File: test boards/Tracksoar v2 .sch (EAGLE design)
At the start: 47 parts, among them IC1 BME280, IC2 74AHC1G125DBV, Y1 16MHZ

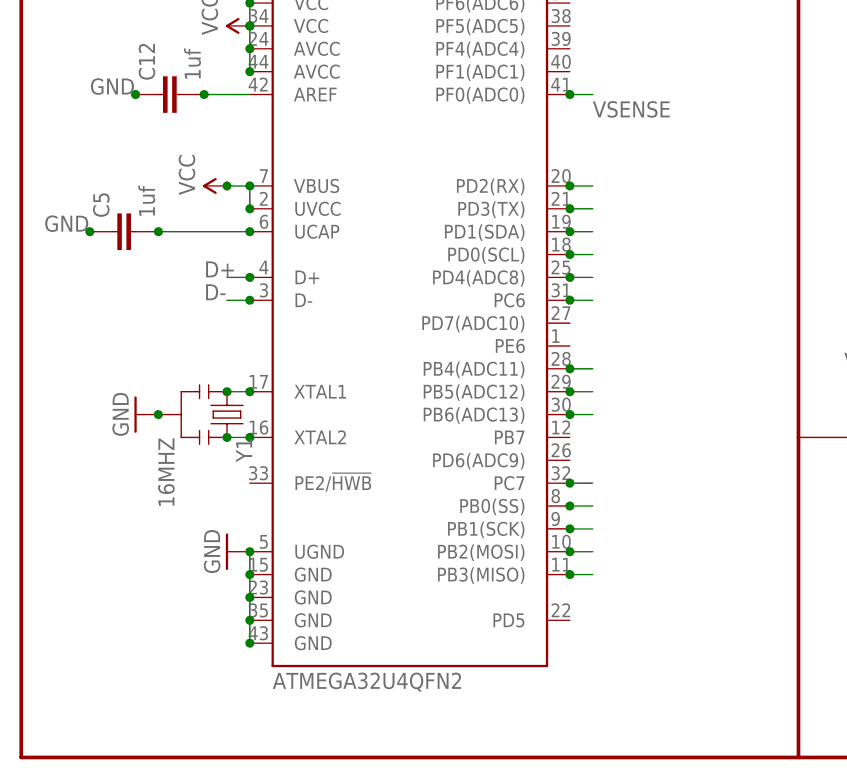
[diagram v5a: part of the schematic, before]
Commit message: Added Pull down to HWB pin
added a 10k pull down resistor to HWB to resolve issues flashing the
boot loader
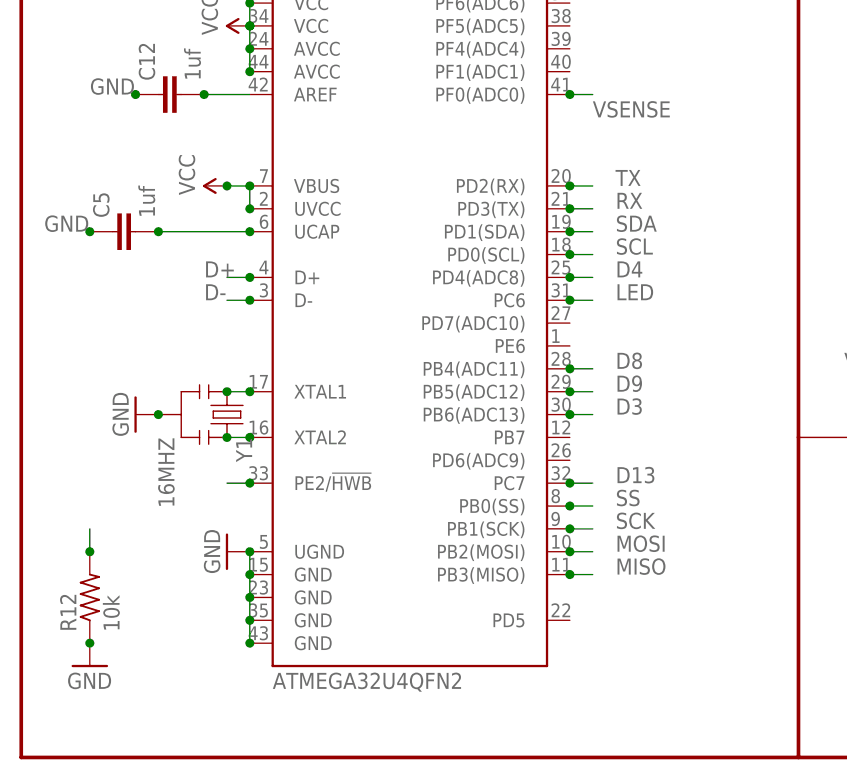
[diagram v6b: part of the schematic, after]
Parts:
- added R12: 10k, adafruit:R-US_R0402
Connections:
- new net HWB: R12.2, U$4.PE2/!HWB
- net GND: now also R12.1
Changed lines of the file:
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@@
 <part name="C14" library="SparkFun-Capacitors" deviceset="CAP" device="0402-CAP" value=".1uf"/>
 <part name="GND21" library="SparkFun-Aesthetics" deviceset="GND" device=""/>
+<part name="R12" library="adafruit" deviceset="R-US_" device="R0402" value="10k"/>
+<part name="GND23" library="SparkFun-Aesthetics" deviceset="GND" device=""/>
 </parts>
 <sheets>
@@
 <instance part="C14" gate="G$1" x="73.66" y="180.34" rot="R270"/>
 <instance part="GND21" gate="1" x="81.28" y="180.34" rot="R90"/>
+<instance part="R12" gate="G$1" x="7.62" y="17.78" rot="R90"/>
+<instance part="GND23" gate="1" x="7.62" y="10.16"/>
 </instances>
 <busses>
@@
 <junction x="78.74" y="180.34"/>
 </segment>
+<segment>
+<pinref part="R12" gate="G$1" pin="1"/>
+<pinref part="GND23" gate="1" pin="GND"/>
+<junction x="7.62" y="12.7"/>
+</segment>
 </net>
 <net name="D3" class="0">
@@
 <pinref part="U$4" gate="G$1" pin="PB6(ADC13)"/>
 <junction x="60.96" y="38.1"/>
+<label x="66.04" y="38.1" size="1.778" layer="95"/>
 </segment>
 </net>
@@
 <pinref part="U$4" gate="G$1" pin="PD4(ADC8)"/>
 <junction x="60.96" y="53.34"/>
+<label x="66.04" y="53.34" size="1.778" layer="95"/>
 </segment>
 </net>
@@
 <pinref part="U$4" gate="G$1" pin="PB3(MISO)"/>
 <junction x="60.96" y="20.32"/>
+<label x="66.04" y="20.32" size="1.778" layer="95"/>
 </segment>
 <segment>
@@
 <pinref part="U$4" gate="G$1" pin="PB2(MOSI)"/>
 <junction x="60.96" y="22.86"/>
+<label x="66.04" y="22.86" size="1.778" layer="95"/>
 </segment>
 <segment>
@@
 <pinref part="U$4" gate="G$1" pin="PB1(SCK)"/>
 <junction x="60.96" y="25.4"/>
+<label x="66.04" y="25.4" size="1.778" layer="95"/>
 </segment>
 <segment>
@@
 <pinref part="U$4" gate="G$1" pin="PB0(SS)"/>
 <junction x="60.96" y="27.94"/>
+<label x="66.04" y="27.94" size="1.778" layer="95"/>
 </segment>
 <segment>
@@
 <pinref part="U$4" gate="G$1" pin="PC6"/>
 <junction x="60.96" y="50.8"/>
+<label x="66.04" y="50.8" size="1.778" layer="95"/>
 </segment>
 </net>
@@
 <pinref part="U$4" gate="G$1" pin="PD1(SDA)"/>
 <junction x="60.96" y="58.42"/>
+<label x="66.04" y="58.42" size="1.778" layer="95"/>
 </segment>
 <segment>
@@
 <pinref part="U$4" gate="G$1" pin="PD0(SCL)"/>
 <junction x="60.96" y="55.88"/>
+<label x="66.04" y="55.88" size="1.778" layer="95"/>
 </segment>
 <segment>
@@
 <pinref part="U$4" gate="G$1" pin="PD2(RX)"/>
 <junction x="60.96" y="63.5"/>
+<label x="66.04" y="63.5" size="1.778" layer="95"/>
 </segment>
 <segment>
@@
 <pinref part="U$4" gate="G$1" pin="PD3(TX)"/>
 <junction x="60.96" y="60.96"/>
+<label x="66.04" y="60.96" size="1.778" layer="95"/>
 </segment>
 <segment>
@@
 <wire x1="60.96" y1="43.18" x2="63.5" y2="43.18" width="0.1524" layer="91"/>
 <junction x="60.96" y="43.18"/>
+<label x="66.04" y="43.18" size="1.778" layer="95"/>
 </segment>
 <segment>
@@
 <wire x1="60.96" y1="40.64" x2="63.5" y2="40.64" width="0.1524" layer="91"/>
 <junction x="60.96" y="40.64"/>
+<label x="66.04" y="40.64" size="1.778" layer="95"/>
 </segment>
 <segment>
@@
 <wire x1="60.96" y1="30.48" x2="63.5" y2="30.48" width="0.1524" layer="91"/>
 <junction x="60.96" y="30.48"/>
+<label x="66.04" y="30.48" size="1.778" layer="95"/>
 </segment>
 </net>
@@
 </segment>
 </net>
+<net name="HWB" class="0">
+<segment>
+<pinref part="U$4" gate="G$1" pin="PE2/!HWB"/>
+<wire x1="25.4" y1="30.48" x2="22.86" y2="30.48" width="0.1524" layer="91"/>
+<junction x="25.4" y="30.48"/>
+</segment>
+<segment>
+<pinref part="R12" gate="G$1" pin="2"/>
+<wire x1="7.62" y1="22.86" x2="7.62" y2="25.4" width="0.1524" layer="91"/>
+<junction x="7.62" y="22.86"/>
+</segment>
+</net>

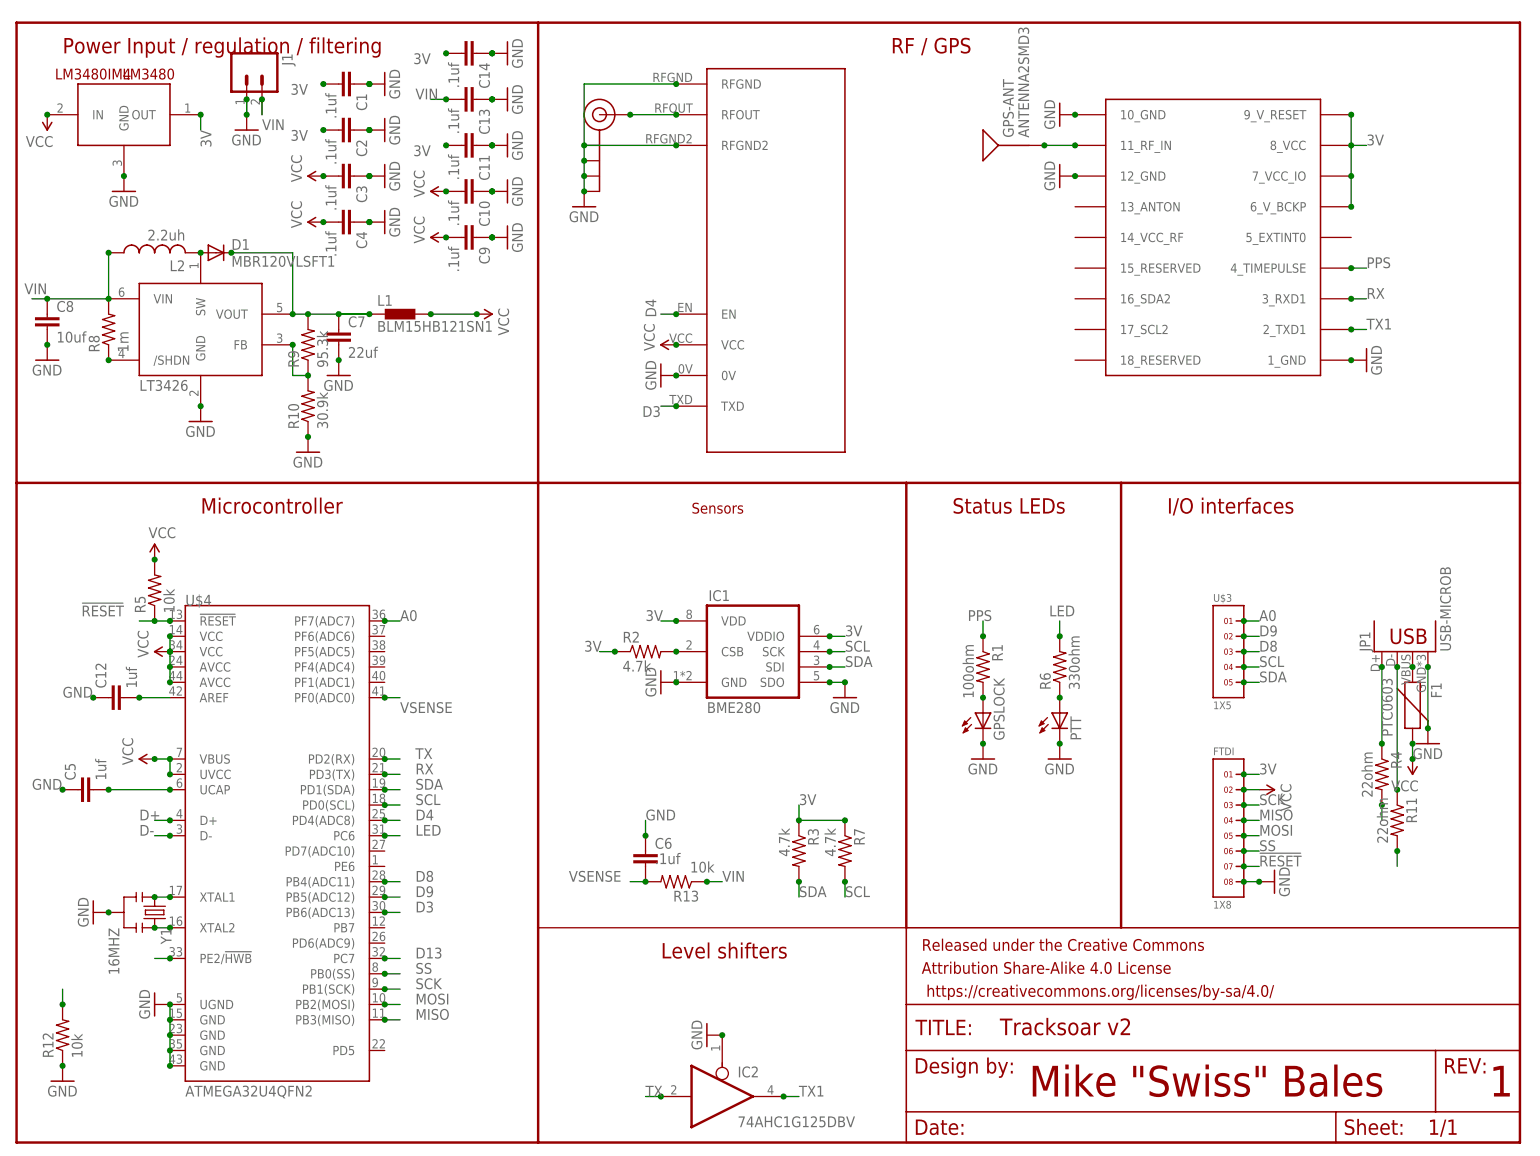
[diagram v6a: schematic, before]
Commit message: Swapped Serial1 RX and TX
Fixed an issue sending / receiving serial between the atmega32u4 and
ublox max m8q by swapping the rx and tx pins on the atmega32u4.
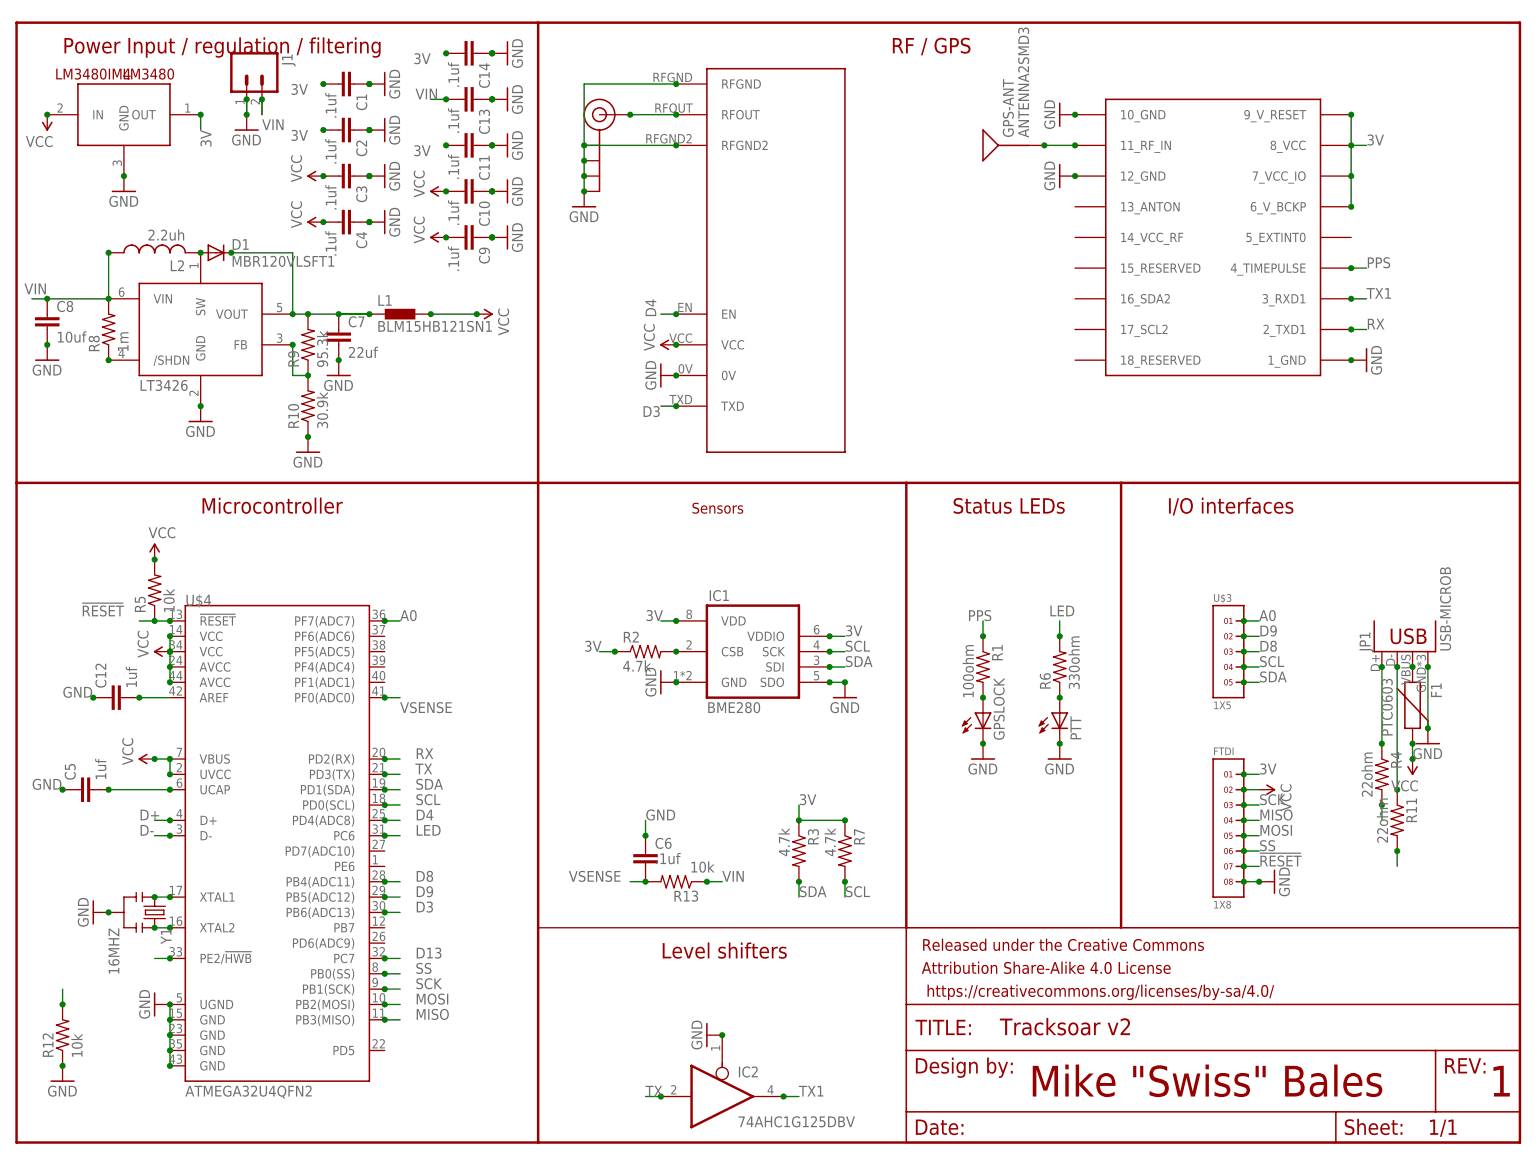
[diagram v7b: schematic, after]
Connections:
- net RX: now also U$1.2_TXD1, U$4.PD2(RX); no longer U$1.3_RXD1, U$4.PD3(TX)
- net TX: now also U$4.PD3(TX); no longer U$4.PD2(RX)
- net TX1: now also U$1.3_RXD1; no longer U$1.2_TXD1
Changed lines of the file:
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@@
 </segment>
 <segment>
-<wire x1="220.98" y1="134.62" x2="223.52" y2="134.62" width="0.1524" layer="91"/>
-<label x="223.52" y="134.62" size="1.778" layer="95"/>
-<pinref part="U$1" gate="G$1" pin="2_TXD1"/>
-<junction x="220.98" y="134.62"/>
+<wire x1="223.52" y1="139.7" x2="220.98" y2="139.7" width="0.1524" layer="91"/>
+<label x="223.52" y="139.7" size="1.778" layer="95"/>
+<pinref part="U$1" gate="G$1" pin="3_RXD1"/>
+<junction x="220.98" y="139.7"/>
 </segment>
 </net>
@@
 <net name="TX" class="0">
 <segment>
+<pinref part="IC2" gate="A" pin="I"/>
+<wire x1="106.68" y1="7.62" x2="104.14" y2="7.62" width="0.1524" layer="91"/>
+<label x="104.14" y="7.62" size="1.778" layer="95"/>
+<junction x="106.68" y="7.62"/>
+</segment>
+<segment>
+<wire x1="60.96" y1="60.96" x2="63.5" y2="60.96" width="0.1524" layer="91"/>
+<pinref part="U$4" gate="G$1" pin="PD3(TX)"/>
+<junction x="60.96" y="60.96"/>
+<label x="66.04" y="60.96" size="1.778" layer="95"/>
+</segment>
+</net>
+<net name="RX" class="0">
+<segment>
 <wire x1="60.96" y1="63.5" x2="63.5" y2="63.5" width="0.1524" layer="91"/>
 <pinref part="U$4" gate="G$1" pin="PD2(RX)"/>
@@
 </segment>
 <segment>
-<pinref part="IC2" gate="A" pin="I"/>
-<wire x1="106.68" y1="7.62" x2="104.14" y2="7.62" width="0.1524" layer="91"/>
-<label x="104.14" y="7.62" size="1.778" layer="95"/>
-<junction x="106.68" y="7.62"/>
-</segment>
-</net>
-<net name="RX" class="0">
-<segment>
-<wire x1="60.96" y1="60.96" x2="63.5" y2="60.96" width="0.1524" layer="91"/>
-<pinref part="U$4" gate="G$1" pin="PD3(TX)"/>
-<junction x="60.96" y="60.96"/>
-<label x="66.04" y="60.96" size="1.778" layer="95"/>
-</segment>
-<segment>
-<wire x1="223.52" y1="139.7" x2="220.98" y2="139.7" width="0.1524" layer="91"/>
-<label x="223.52" y="139.7" size="1.778" layer="95"/>
-<pinref part="U$1" gate="G$1" pin="3_RXD1"/>
-<junction x="220.98" y="139.7"/>
-</segment>
-</net>
+<wire x1="220.98" y1="134.62" x2="223.52" y2="134.62" width="0.1524" layer="91"/>
+<label x="223.52" y="134.62" size="1.778" layer="95"/>
+<pinref part="U$1" gate="G$1" pin="2_TXD1"/>
+<junction x="220.98" y="134.62"/>
+</segment>
+</net>
